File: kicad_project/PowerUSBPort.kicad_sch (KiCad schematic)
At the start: 12 parts, among them J3 USB4105-GF-A, U8 USBLC6-2SC6, U9 LD1117S33TR

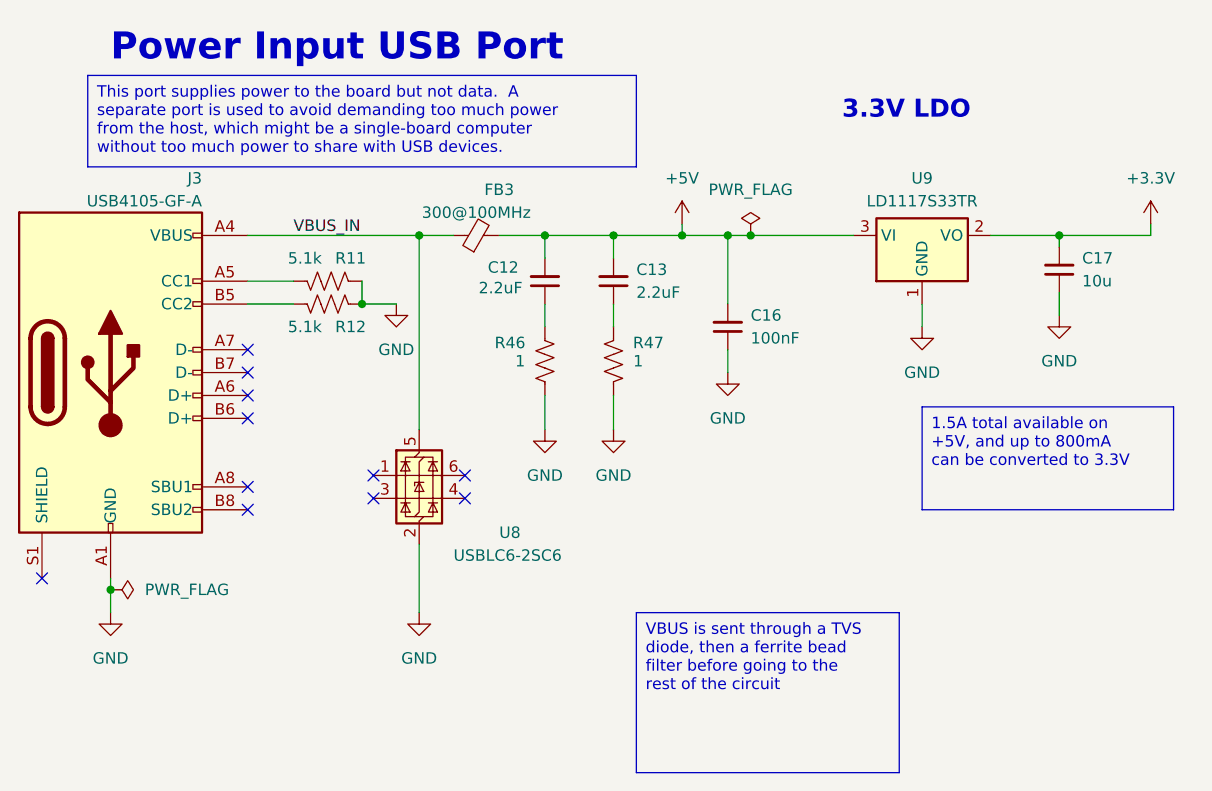
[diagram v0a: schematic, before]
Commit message: Switch out multiplexer, start switch FX2LP out for RP2040
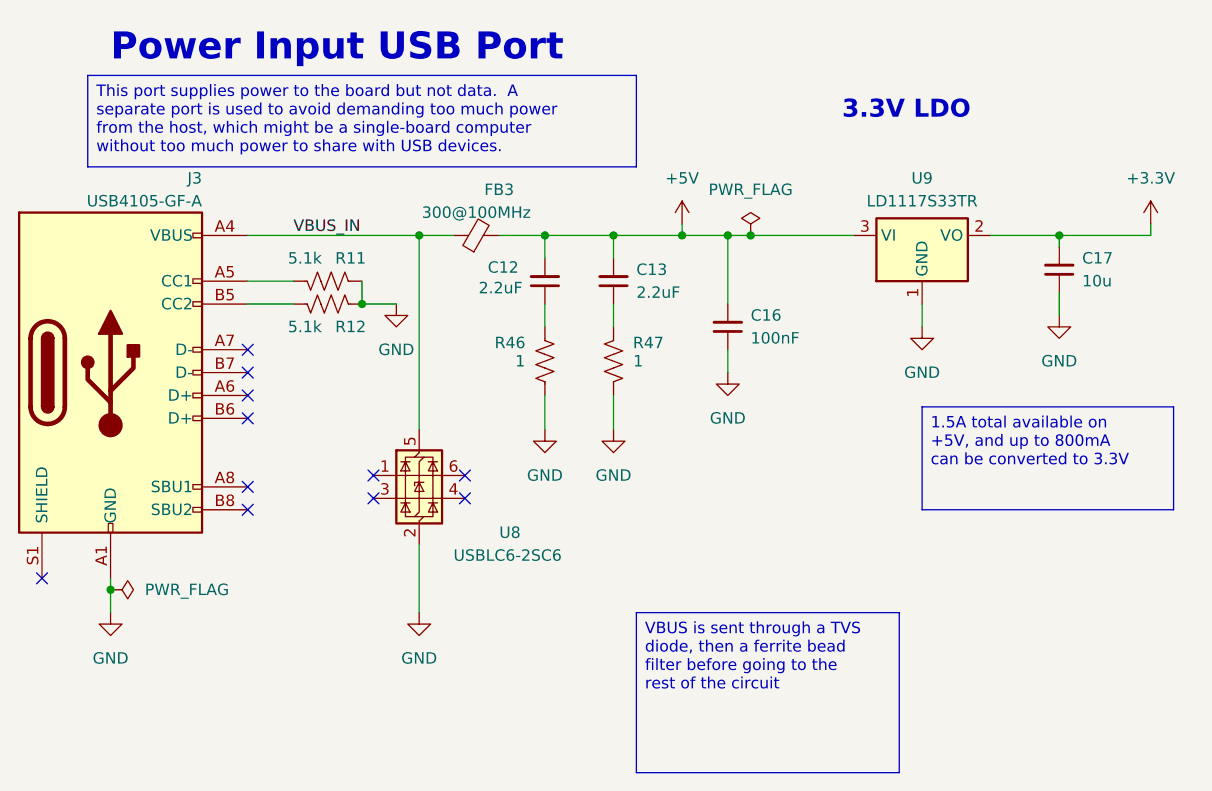
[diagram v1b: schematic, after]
